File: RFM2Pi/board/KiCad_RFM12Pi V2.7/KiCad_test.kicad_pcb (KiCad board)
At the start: 2 copper layers, 30 x 30 mm, 15 parts, among them CON1 AVR-ISP-6, IC1 ATMEGA328P-A, IC2 ATMEGA328P-A, P1 CONN_02X05_RasPi_GPIO, U1 RFM12

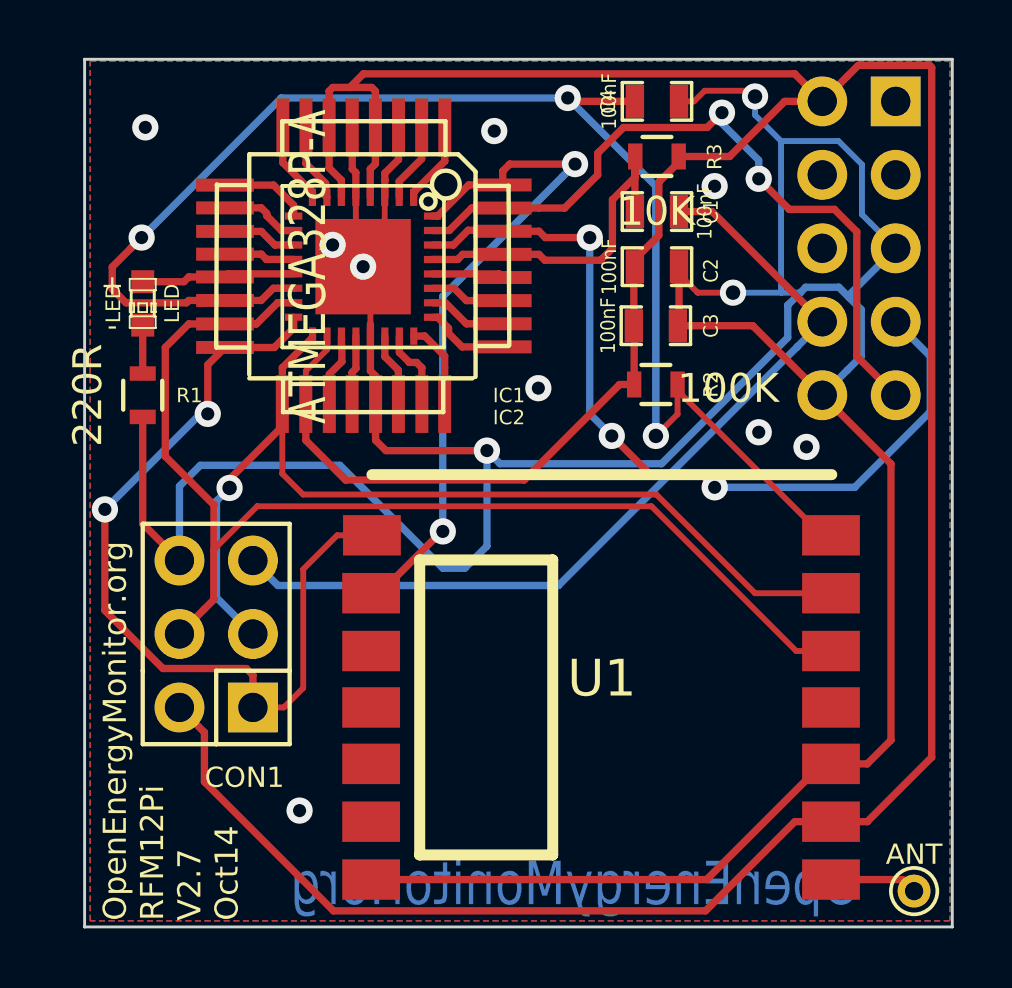
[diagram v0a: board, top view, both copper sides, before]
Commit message: update kicad and remove rfm12ppi frmware, see openenergymonitor/rfm12pi repo for latest firmware
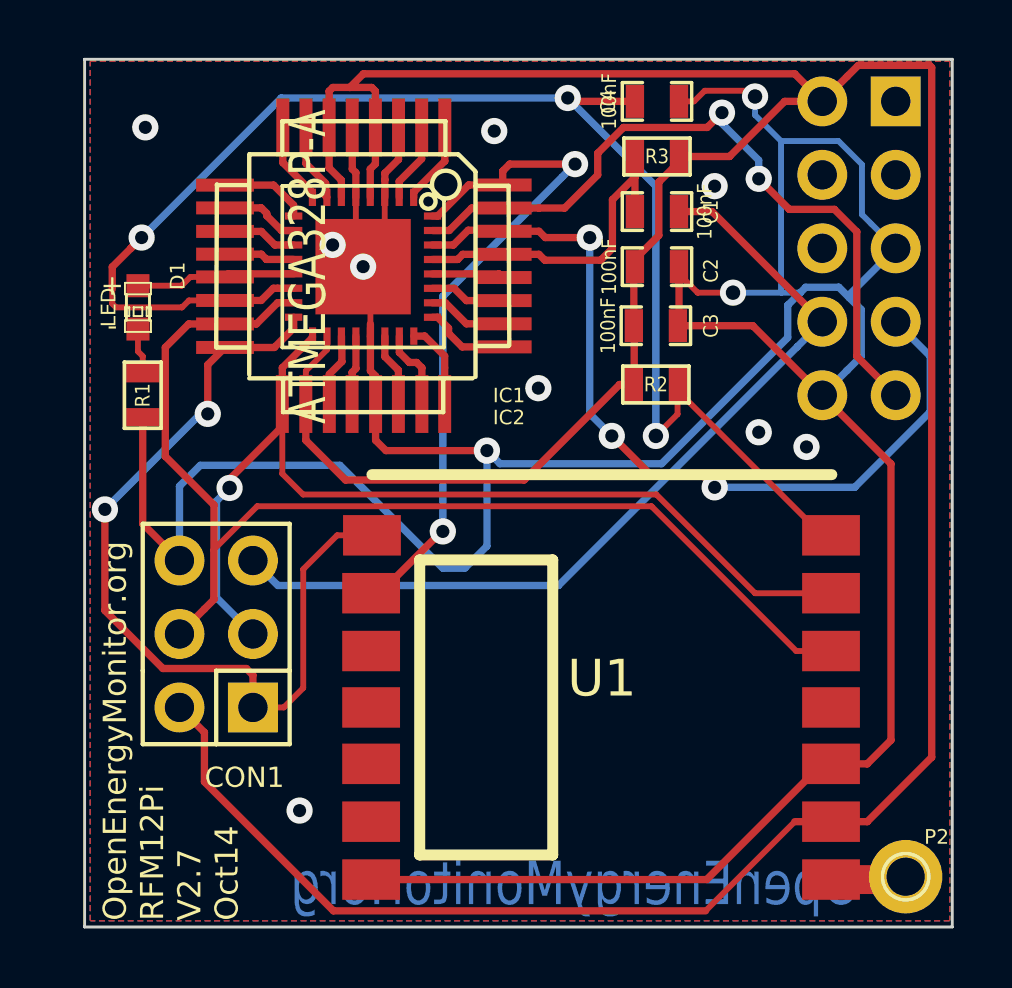
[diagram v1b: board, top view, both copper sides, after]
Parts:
- removed ANT: CONN_01X01, Connect:PINTST
- removed LED: LED, LEDs:LED-0603
- added D1: LED, LEDs:LED-0603, F.Cu at (140.8, 101.7)
- added P2: CONN_01X01, ant:PINTST, F.Cu at (167.3, 121.4)
- R1, R2, R3: footprint Resistors_SMD:R_0603 -> SMD_Packages:SMD-0603
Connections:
- IC2 pad 33: GND -> (no net)
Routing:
- net Net-(P2-Pad1): track 3.04 -> 2.47 mm
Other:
- net class Ant added: clearance 0.254, trace_width 1, via_dia 0.9064, via_drill 0.5
- net class Default: clearance 0.2032 -> 0.254
- rule trace_clearance: 0.2032 -> 0.254
